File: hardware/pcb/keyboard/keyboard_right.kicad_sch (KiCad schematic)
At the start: 9 parts, among them J1 SM04B-SRSS-TB, J2 PJ320D, J4 FH34SRJ-10S-0.5SH, SW29 SW_Push, U3 nRF52840_holyiot_18010, U5 DT1446-04S

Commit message: Init STM32G0 PCB
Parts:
- removed J5: ~, ec_parts:PinHeader_1x04_P2.54mm_top_only, symbol Connector_Generic:Conn_01x04
- removed R9: 10k, PCM_Resistor_SMD_AKL:R_0603_1608Metric_Pad0.98x0.95mm, symbol Device:R
- removed U3: nRF52840_holyiot_18010, PCM_marbastlib-various:nRF52840_holyiot_18010_HS_simple, symbol PCM_marbastlib-various:nRF52840_holyiot_18010
- removed U5: DT1446-04S, PCM_Package_TO_SOT_SMD_AKL:SOT-363_SC-70-6_Handsoldering, symbol Power_Protection:SRV05-4
- added C1, C4: 0.1uF, PCM_Capacitor_SMD_AKL:C_0603_1608Metric_Pad1.05x0.95mm, symbol Device:C
- added C20: 1uF, PCM_Capacitor_SMD_AKL:C_0603_1608Metric_Pad1.05x0.95mm, symbol Device:C
- added C5: 4.7u, PCM_Capacitor_SMD_AKL:C_0603_1608Metric_Pad1.05x0.95mm, symbol Device:C
- added C6, C7: 22p, PCM_Capacitor_SMD_AKL:C_0603_1608Metric_Pad1.05x0.95mm, symbol Device:C
- added D1: 1N5819, PCM_Diode_SMD_AKL:D_SOD-323_HandSoldering, symbol PCM_Diode_Schottky_AKL:1N5818
- added F1: 500mA, PCM_Fuse_AKL:Fuse_1206_3216Metric, symbol Device:Polyfuse
- added H17: ~, ec_parts:PinHeader_1x01, symbol Mechanical:MountingHole_Pad
- added J3: HRO_TYPE-C-31-M-12, ec_parts:USB_C_Receptacle_HRO_TYPE-C-31-M-12, symbol ec_parts:USB_C_Receptacle_USB2.0
- added L1: 60R@100MHz, PCM_Inductor_SMD_AKL:L_1206_3216Metric, symbol Unified-Daughterboard-rescue:L_Core_Ferrite-Device
- added R9: 10k, PCM_Resistor_SMD_AKL:R_0603_1608Metric_Pad0.98x0.95mm, symbol Device:R
- added R9: 5.6k, PCM_Resistor_SMD_AKL:R_0603_1608Metric_Pad0.98x0.95mm, symbol Device:R
- added R9 (x2): 5.1k, PCM_Resistor_SMD_AKL:R_0603_1608Metric_Pad0.98x0.95mm, symbol Device:R
- added RN3: 100 R_Array_Convex_4x0603, PCM_Resistor_SMD_AKL:R_Array_Concave_4x0603, symbol PCM_Resistor_AKL:R_4x0612_Convex
- added TP1: ~, ec_parts:PinHeader_1x04_P2.54mm_test_pad, symbol Connector_Generic:Conn_01x04
- added U3: DT1446-04S, PCM_Package_TO_SOT_SMD_AKL:SOT-363_SC-70-6_Handsoldering, symbol Power_Protection:SRV05-4
- added U4: XC6220B331MR-G, PCM_Package_TO_SOT_SMD_AKL:SOT-23-5, symbol Regulator_Linear:AP2112K-3.3
- added U5: STM32G0B1KETx, PCM_Package_QFP_AKL:LQFP-32_7x7mm_P0.8mm, symbol MCU_ST_STM32G0:STM32G0B1KETx
- added Y1: 32.768kHz, PCM_Crystal_AKL:Crystal_SMD_3215-2Pin_3.2x1.5mm, symbol Device:Crystal
- C21: value ~ -> 1uF; footprint PCM_Capacitor_SMD_AKL:C_0603_1608Metric_Pad1.08x0.95mm -> PCM_Capacitor_SMD_AKL:C_0603_1608Metric_Pad1.05x0.95mm; Comment Don't need -> (none)
- SW29: value SW_Push -> PTS845
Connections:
- net SWDCLK is gone; now on net +5V: J1.1 (Pin_1)
- net +3V3: now also C20.1, C4.1, C5.1, U4.5 (VOUT), U5.4 (VDD); no longer J1.4 (Pin_4)
- net +5V: now also C21.1, D1.1 (K), TP1.1 (Pin_1), U3.5 (VP), U4.1 (VIN), U4.3 (EN)
- net ACCS_1: now also U5.26 (PA15)
- net ACCS_2: now also U5.27 (PB3)
- net ACCS_3: now also U5.28 (PB4)
- net ACCS_4: now also U5.29 (PB5)
- net ACCS_5: now also U5.30 (PB6)
- net ACCS_6: now also U5.31 (PB7)
- net ACCS_7: now also U5.21 (PA10/UCPD1_DBCC2)
- net ACCS_8: now also U5.20 (PC6)
- net ADC: now also U5.12 (PA5)
- net CHARGE_RST: now also U5.14 (PA7)
- net CSEL0: now also U5.8 (PA1)
- net CSEL1: now also U5.9 (PA2)
- net CSEL2: now also U5.10 (PA3)
- net CSEL_EN: now also U5.15 (PB0)
- net D+: now also J3.A6 (D+), J3.B6 (D+), U3.3 (IO2), U5.23 (PA12/PA10)
- net D-: now also J3.A7 (D-), J3.B7 (D-), U3.4 (IO3), U5.22 (PA11/PA9)
- net GND: now also J1.4 (Pin_4), C1.1, C20.2, C4.2, C5.2, C6.1, C7.1, J3.A1 (GND), J3.A12 (GND), J3.B1 (GND), J3.B12 (GND), L1.1, R9.2, R9.2, R9.2, TP1.4 (Pin_4), U3.2 (VN), U4.2 (GND), U5.5 (VSS); no longer J1.2 (Pin_2)
- net GNDPWR: now also H17.1, J3.S1 (SHIELD), L1.2
- net ROW0: now also RN3.4 (R4.1)
- net ROW1: now also RN3.3 (R3.1)
- net ROW2: now also RN3.2 (R2.1)
- net ROW3: now also RN3.1 (R1.1)
- net SWDIO: now also J1.2 (Pin_2), TP1.2 (Pin_2), U5.24 (PA13); no longer J1.3 (Pin_3)
- net VBUS_DEC: now also R9.1, R9.2, U5.7 (PA0)
- net RESET renamed NRST
- net NRST: now also C1.2, U5.6 (PF2); no longer C21.1
- net SCL renamed USART_TX
- net USART_TX: now also U3.6 (IO4), U5.32 (PB8)
- net SDA renamed USART_RX
- net USART_RX: now also U3.1 (IO1), U5.1 (PB9)
- new net: D1.2 (A), F1.1, R9.1
- new net: J3.A5 (CC1), R9.1
- new net: J3.B5 (CC2), R9.1
- new net ADC1_IN4: U5.11 (PA4)
- new net ADC1_IN6: U5.13 (PA6)
- new net OSC32_IN: C6.2, U5.2 (PC14), Y1.1
- new net OSC32_OUT: C7.2, U5.3 (PC15), Y1.2
- new net SWCLK: J1.3 (Pin_3), TP1.3 (Pin_3), U5.25 (PA14)
- new net TX0: RN3.5 (R4.2), U5.19 (PA9/UCPD1_DBCC1)
- new net TX1: RN3.6 (R3.2), U5.18 (PA8)
- new net TX2: RN3.7 (R2.2), U5.17 (PB2)
- new net TX3: RN3.8 (R1.2), U5.16 (PB1)
- new net VBUS: F1.2, J3.A4 (VBUS), J3.A9 (VBUS), J3.B4 (VBUS), J3.B9 (VBUS)
- no-connect marks 3 -> 11
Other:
- sheet key_matrix renamed analog&key matrix
- removed sheet analog
- removed sheet usb_power
- note added: "2.54mm pitch test points"
- note added: "Adjust Col, Row pins to resistor array and Mux."
- note added: "ESD Protection"
- note added: "JST-SH"
- note added: "Pin functionalities. PA15|USART2_RX| | | | |SPI1_NSS | |SPI3_NSS PB03| | | |I2C2_SCL|I2C3_SCL|SPI1_SCK | |SPI3_SCK PB04| | | |I2C2_SDA|I2C3_SDA|SPI1_MISO| |SPI3_MISO PB05| | |I2C1_SMBA| | |SPI1_MOSI| |SPI3_MOSI PB06|USART1_TX| |I2C1_SCL | | | |SPI2_MISO| PB07|USART1_RX| |I2C1_SDA | | | |SPI2_MOSI| PA10|USART1_RX| |I2C1_SDA |I2C2_SDA| | |SPI2_MOSI| PC06|"
- note added: "Probe connectors"
- note added: "STM32G0B1KxT Series"
- note added: "TRRS Connector"
- note added: "USB&Power"
- note removed: "C5 Don't need!."
- note removed: "Provde 2 connector for SWD. - JST SH 1x04 connector. - 2.54mm pitch test point."
- note removed: "Split I2C"

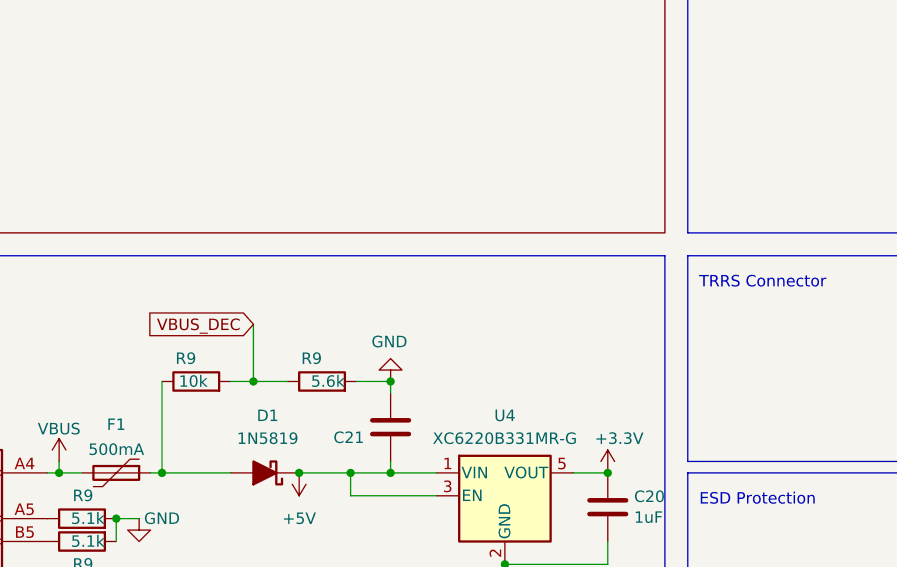
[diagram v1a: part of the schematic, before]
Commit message: Fix capacitor, resistor values
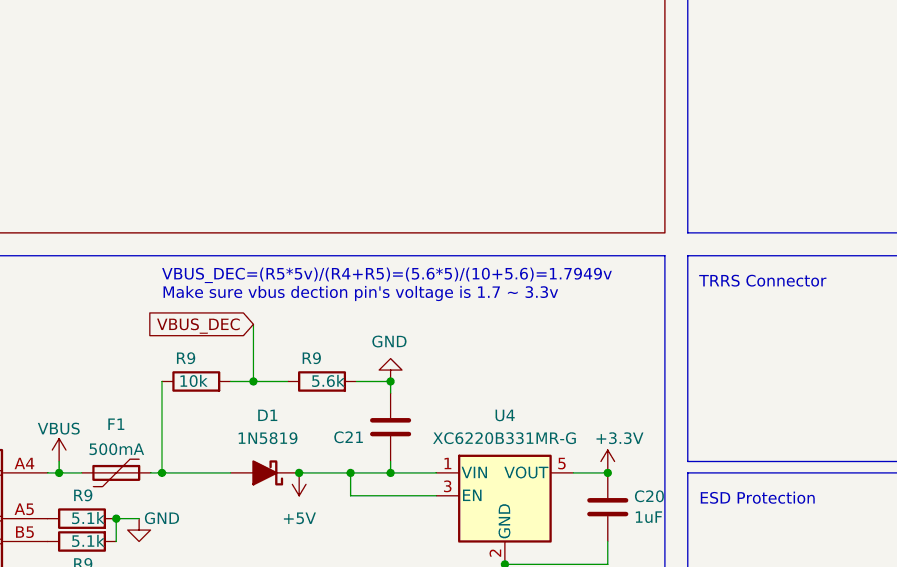
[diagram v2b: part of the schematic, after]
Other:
- note added: "VBUS_DEC=(R5*5v)/(R4+R5)=(5.6*5)/(10+5.6)=1.7949v Make sure vbus dection pin's voltage is 1.7 ~ 3.3v"
- title: (none) -> Corne EEC - Keyboard Right
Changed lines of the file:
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@@
   (paper "A4")
   (title_block
-    (date "2023-07-07")
+    (title "Corne EEC - Keyboard Right")
+    (date "2023-07-18")
     (rev "1.0")
     (comment 2 "MIT License")
@@
     (effects (font (face "Hack Nerd Font") (size 1.5 1.5)) (justify left bottom))
   )
+  (text "VBUS_DEC=(R5*5v)/(R4+R5)=(5.6*5)/(10+5.6)=1.7949v\nMake sure vbus dection pin's voltage is 1.7 ~ 3.3v"
+    (at 57.15 99.06 0)
+    (effects (font (face "Hack Nerd Font") (size 1.27 1.27)) (justify left bottom))
+  )
   (text "2.54mm pitch test points" (at 143.51 175.26 0)

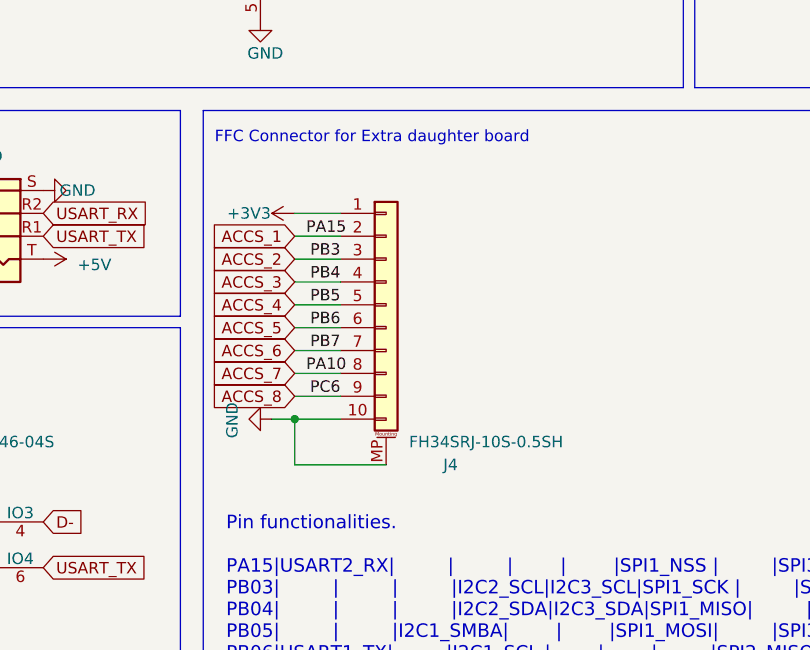
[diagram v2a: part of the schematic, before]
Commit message: roate FFC Connector
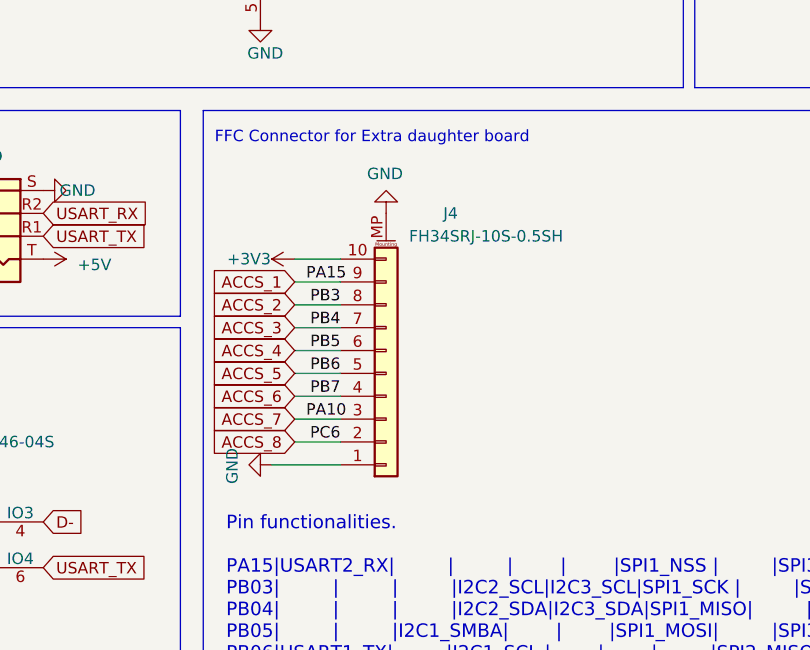
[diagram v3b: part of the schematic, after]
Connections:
- net +3V3: now also J4.10 (Pin_10); no longer J4.1 (Pin_1)
- net ACCS_1: now also J4.9 (Pin_9); no longer J4.2 (Pin_2)
- net ACCS_2: now also J4.8 (Pin_8); no longer J4.3 (Pin_3)
- net ACCS_3: now also J4.7 (Pin_7); no longer J4.4 (Pin_4)
- net ACCS_4: now also J4.6 (Pin_6); no longer J4.5 (Pin_5)
- net ACCS_5: now also J4.5 (Pin_5); no longer J4.6 (Pin_6)
- net ACCS_6: now also J4.4 (Pin_4); no longer J4.7 (Pin_7)
- net ACCS_7: now also J4.3 (Pin_3); no longer J4.8 (Pin_8)
- net ACCS_8: now also J4.2 (Pin_2); no longer J4.9 (Pin_9)
- net GND: now also J4.1 (Pin_1); no longer J4.10 (Pin_10)

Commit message: init
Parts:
- removed C1: 0.1uF, PCM_Capacitor_SMD_AKL:C_0603_1608Metric_Pad1.05x0.95mm, symbol Device:C
- removed C6, C7: 22p, PCM_Capacitor_SMD_AKL:C_0603_1608Metric_Pad1.05x0.95mm, symbol Device:C
- removed J4: FH34SRJ-10S-0.5SH, ec_parts:HRS_FH34SRJ-10S-0.5SH(50), symbol Connector_Generic_MountingPin:Conn_01x10_MountingPin
- removed Y1: 32.768kHz, PCM_Crystal_AKL:Crystal_SMD_3215-2Pin_3.2x1.5mm, symbol Device:Crystal
- added C14: 10n, PCM_Capacitor_SMD_AKL:C_0603_1608Metric, symbol Device:C
- added J4: Conn_01x08_MountingPin, ec_parts:CONN8_FH34SRJ_HIR, symbol Connector_Generic_MountingPin:Conn_01x08_MountingPin
- added R1: 1k, PCM_Resistor_SMD_AKL:R_0603_1608Metric_Pad0.98x0.95mm, symbol Device:R
- added R10, R9: 10k, PCM_Resistor_SMD_AKL:R_0603_1608Metric, symbol Device:R
- added U6: 24FC01T-I/OT, ec_parts:SOT-23-5_2P9X1P6_MCH, symbol 24FC01T-I/OT:24FC01T-I_OT
- renumbered C21 to C8, C20 to C9, R9 to R2, R9 to R3, R9 to R4, R9 to R5
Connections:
- net +3V3: now also J1.1 (Pin_1), TP1.1 (Pin_1), C14.2, J4.1 (Pin_1), R10.1, R9.2, U6.4 (VCC)
- net +5V: no longer J1.1 (Pin_1), TP1.1 (Pin_1)
- net GND: now also C14.1, J4.8 (Pin_8), U6.2 (VSS), U6.5 (WP)
- net ACCS_1 renamed PA15
- net PA15: now also J4.2 (Pin_2)
- net ACCS_2 renamed PB3
- net PB3: now also J4.3 (Pin_3)
- net ACCS_3 renamed PB4
- net PB4: now also J4.4 (Pin_4)
- net ACCS_4 renamed PB5
- net PB5: now also J4.5 (Pin_5)
- net ACCS_5 renamed I2C1_SCL
- net I2C1_SCL: now also R10.2, U6.1 (SCL)
- net ACCS_6 renamed I2C1_SDA
- net I2C1_SDA: now also R9.1, U6.3 (SDA)
- net ACCS_7 renamed PA10
- net PA10: now also J4.6 (Pin_6)
- net ACCS_8 renamed PC6
- net PC6: now also J4.7 (Pin_7)
- net OSC32_IN: no longer names the net of U5.2 (PC14)
- net OSC32_IN: now also R1.2
- net OSC32_OUT: no longer names the net of U5.3 (PC15)
- net OSC32_OUT: now also R1.1
- no-connect marks 11 -> 12
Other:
- note added: "Pin functionalities. PA15| | | |SPI1_NSS |SPI3_NSS PB03| |I2C2_SCL|I2C3_SCL|SPI1_SCK |SPI3_SCK PB04| |I2C2_SDA|I2C3_SDA|SPI1_MISO|SPI3_MISO PB05|I2C1_SMBA| | |SPI1_MOSI|SPI3_MOSI PA10|I2C1_SDA |I2C2_SDA| | | PC06|"
- note removed: "Pin functionalities. PA15|USART2_RX| | | | |SPI1_NSS | |SPI3_NSS PB03| | | |I2C2_SCL|I2C3_SCL|SPI1_SCK | |SPI3_SCK PB04| | | |I2C2_SDA|I2C3_SDA|SPI1_MISO| |SPI3_MISO PB05| | |I2C1_SMBA| | |SPI1_MOSI| |SPI3_MOSI PB06|USART1_TX| |I2C1_SCL | | | |SPI2_MISO| PB07|USART1_RX| |I2C1_SDA | | | |SPI2_MOSI| PA10|USART1_RX| |I2C1_SDA |I2C2_SDA| | |SPI2_MOSI| PC06|"
- moved on the sheet: SW29
